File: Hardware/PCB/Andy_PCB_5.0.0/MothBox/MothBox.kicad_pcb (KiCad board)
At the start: 2 copper layers, 237 x 140.5 mm, 143 parts, among them P1 Raw Input, P2 12V Regulated Input, P3 Input to regulator, P4 External Attractor, Q1 BC817, Q10 BC817, Q11 BC817, Q2 TJ10S04M3L,LXHQ, Q4 BC817, Q5 TJ10S04M3L,LXHQ, Q6 BC817, Q7 TJ10S04M3L,LXHQ, Q8 BC817, Q9 BC817, U1 Days, U10 IRF9335TRPBF, U11 IRF9335TRPBF, U12 IRF9335TRPBF, U13 IRF9335TRPBF, U16 Female Inv Socket Pi 2.54-2*20, U17 GPs 5 pin PM2.54-1*5, U18 RASPBERRY_PI_4B_4GB, U19 INA219BIDCNT, U2 Hours1, U3 XL4015E1, U5 RASPBERRY_PI_5, U6 Hours2, U7 Modes, U8 CD74HC4067M96E4, U9 CD74HC4067M96E4

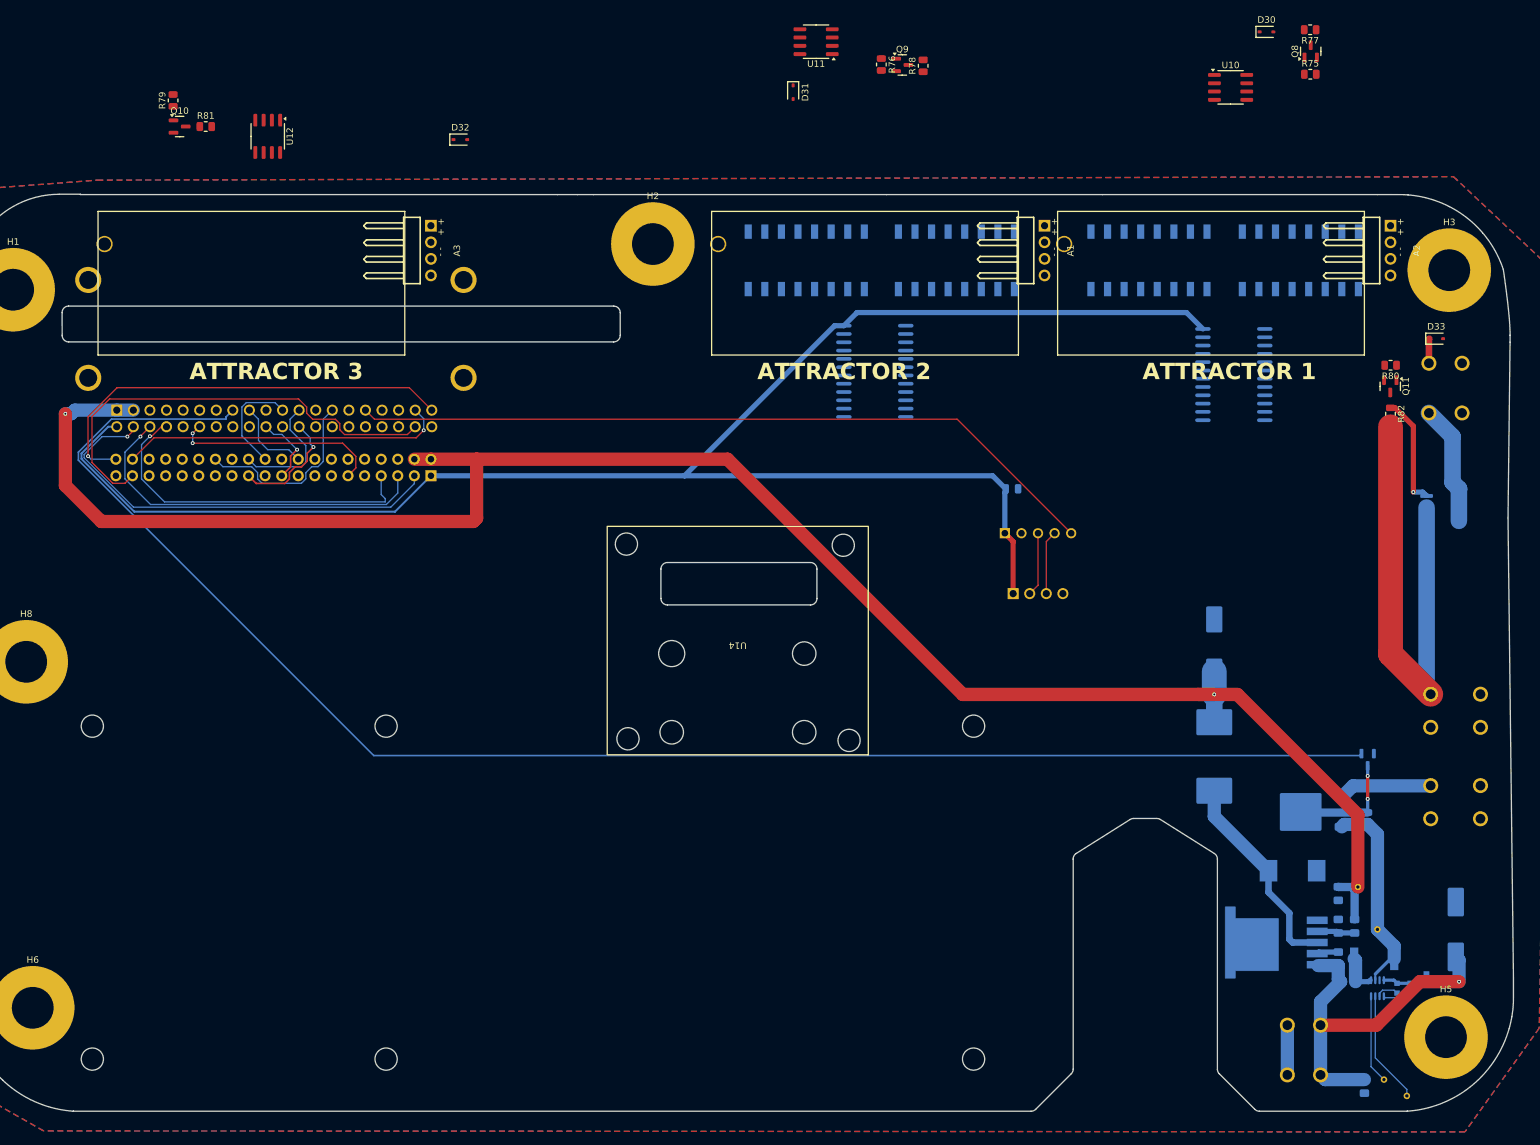
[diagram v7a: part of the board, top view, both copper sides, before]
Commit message: Wired all attractors
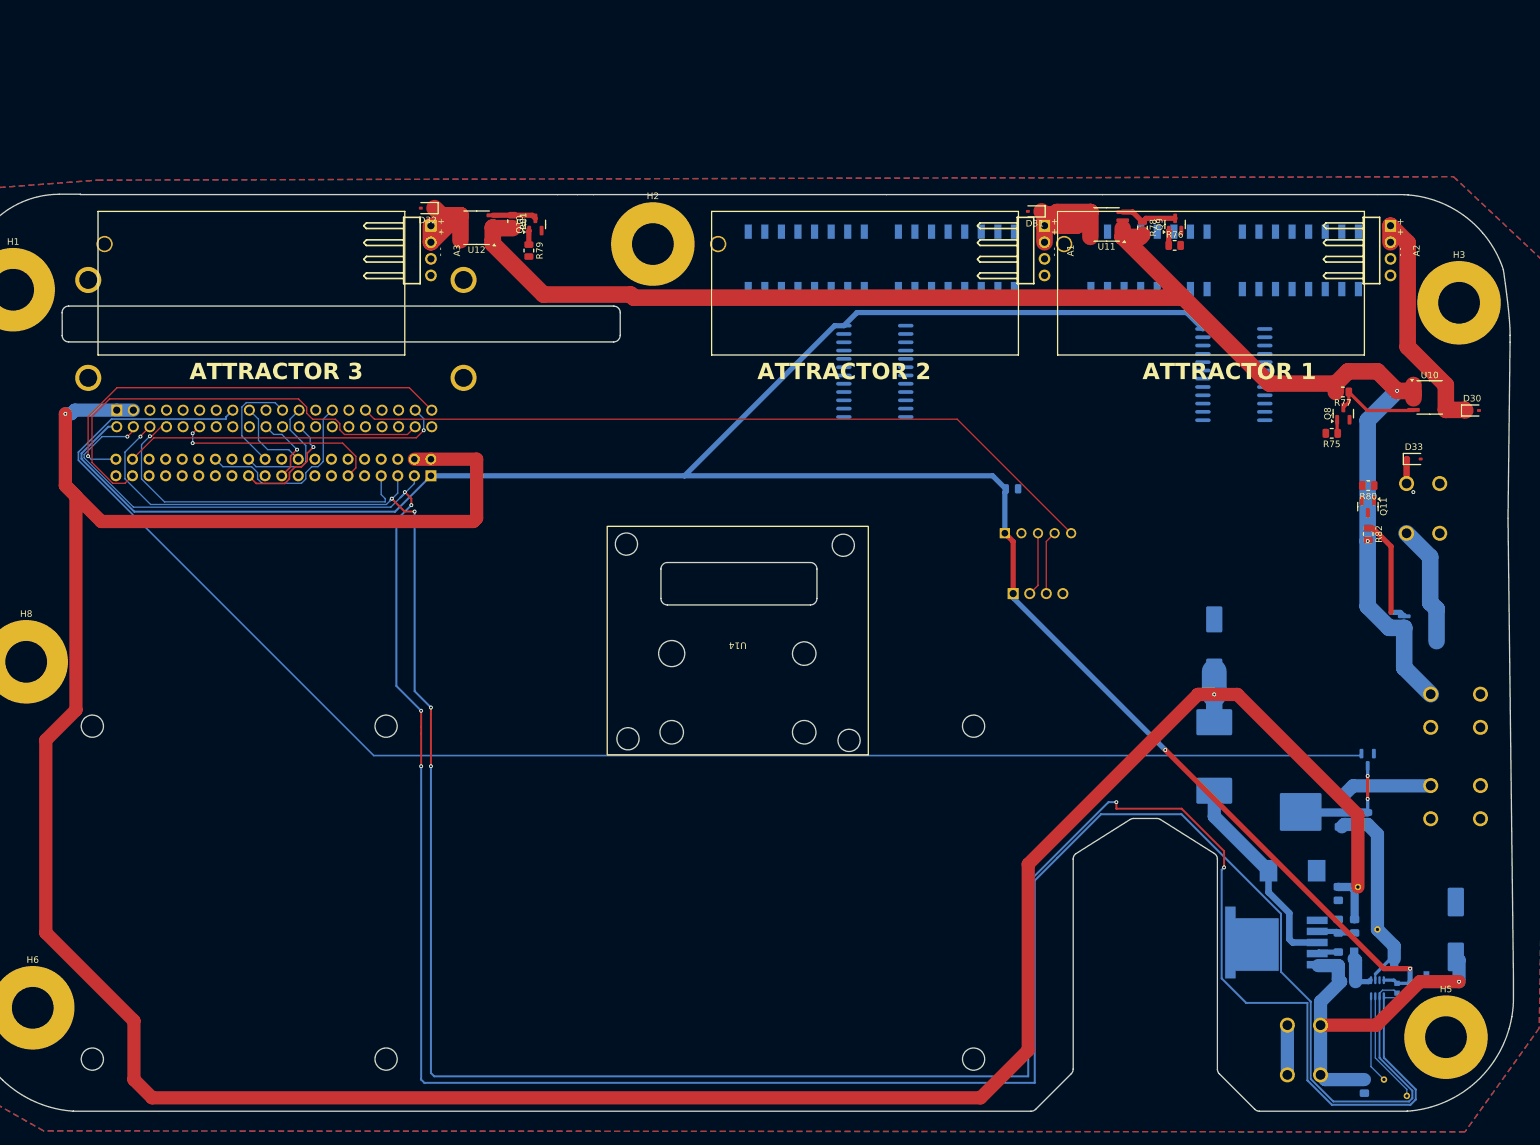
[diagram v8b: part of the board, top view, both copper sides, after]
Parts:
- moved D30 66.0 mm to (262.0, 96.3)
- moved R79 59.2 mm to (117.5, 71.8), turned to -90 degrees
- moved Q10 56.5 mm to (118.5, 67.8), turned to 90 degrees
- moved U10 56.4 mm to (255.5, 94.3)
- moved Q8 55.7 mm to (242.3, 96.7)
- moved R77 55.7 mm to (242.2, 93.4)
- moved R75 55.1 mm to (240.5, 99.8), turned to 180 degrees
- moved R76 52.8 mm to (216.4, 71.0), turned to 0 degrees
- moved U11 52.6 mm to (206.0, 67.8)
- moved R81 49.2 mm to (115.0, 67.3), turned to -90 degrees
- moved Q9 48.4 mm to (216.5, 67.8), turned to 90 degrees
- moved R78 41.8 mm to (211.5, 68.3), turned to -90 degrees
- moved D31 41.3 mm to (195.0, 65.8), turned to 180 degrees
- moved U12 34.9 mm to (109.5, 68.3), turned to 180 degrees
- moved D33 18.7 mm to (253.1, 103.7)
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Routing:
- net SCL: track 60.8 -> 395.3 mm, vias 1 -> 7
- net SDA: track 70.1 -> 399.7 mm, vias 1 -> 5
- net +5V: track 292.8 -> 473.0 mm
- net +12V: track 72.4 -> 232.3 mm, vias 0 -> 2
- net +3.3V: track 270.1 -> 357.4 mm, vias 0 -> 2
- net /UV LED PCB/+12V_PCB1: track 0.00 -> 37.3 mm
- net /UV LED PCB/+12V_PCB2: track 0.00 -> 24.0 mm
- net /UV LED PCB/+12V_PCB3: track 0.00 -> 17.0 mm
- net Net-(Q8-C): track 0.00 -> 13.9 mm
- net Net-(Q9-C): track 0.00 -> 8.86 mm
- net Net-(Q10-C): track 0.00 -> 6.72 mm
- net Net-(Q9-B): track 0.00 -> 2.30 mm
- net Net-(Q10-B): track 0.00 -> 2.17 mm
- net Net-(Q8-B): track 0.00 -> 2.12 mm
